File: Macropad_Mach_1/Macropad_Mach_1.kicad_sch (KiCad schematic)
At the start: 39 parts, among them J1 Conn_01x12, J2 Conn_01x12, SW1 RotaryEncoder_Switch_MP

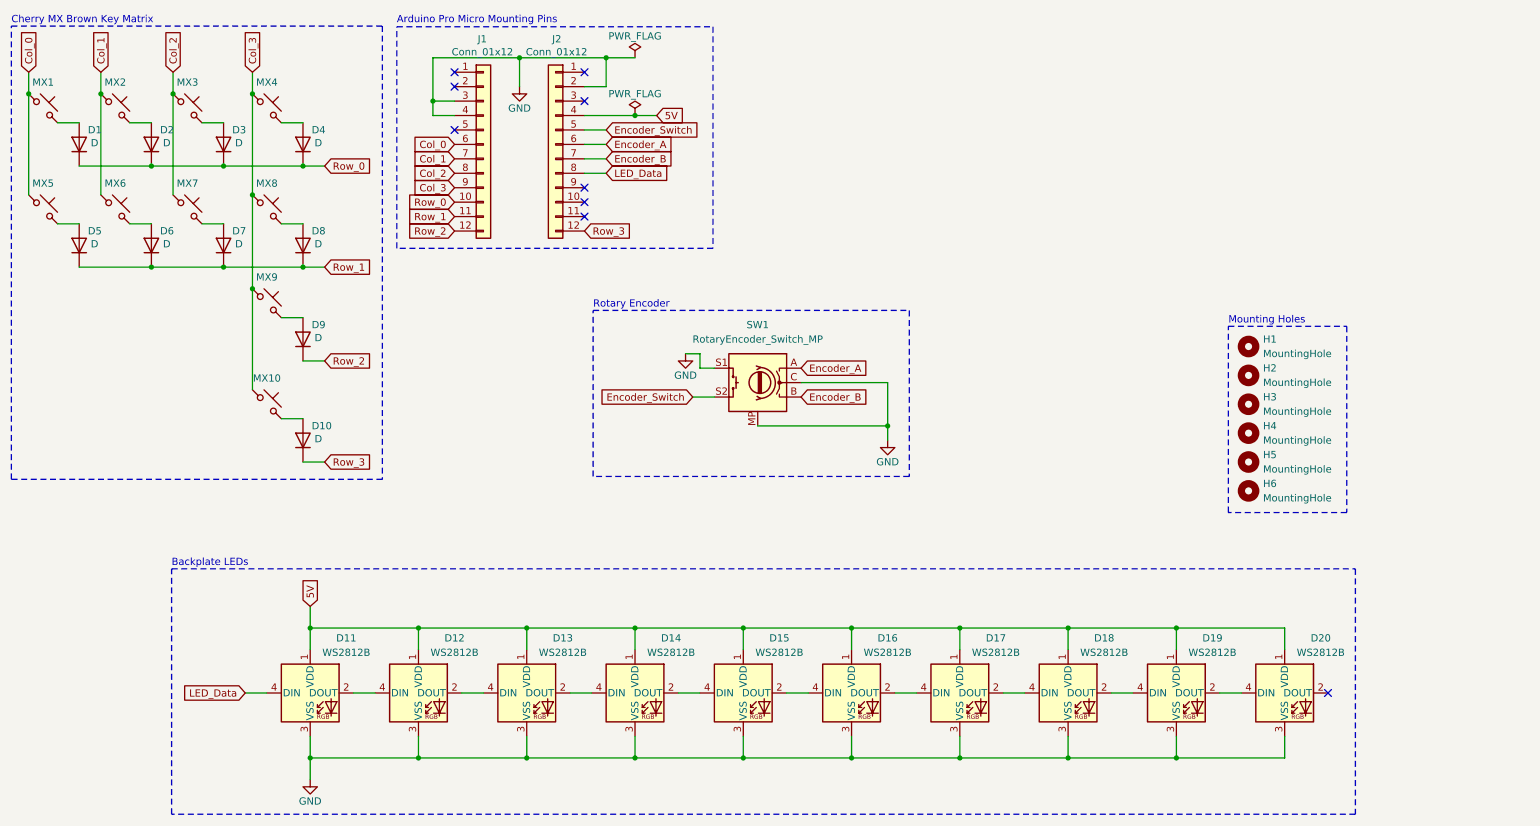
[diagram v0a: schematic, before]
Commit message: feat: update PCB with APA102-2020 LEDs, keyboard layout, and encoder
- Replaced LEDs with APA102-2020
- Created the keyboard layout
- Added Edgecuts
- Routed the keys
- Integrated the encoder into the layout
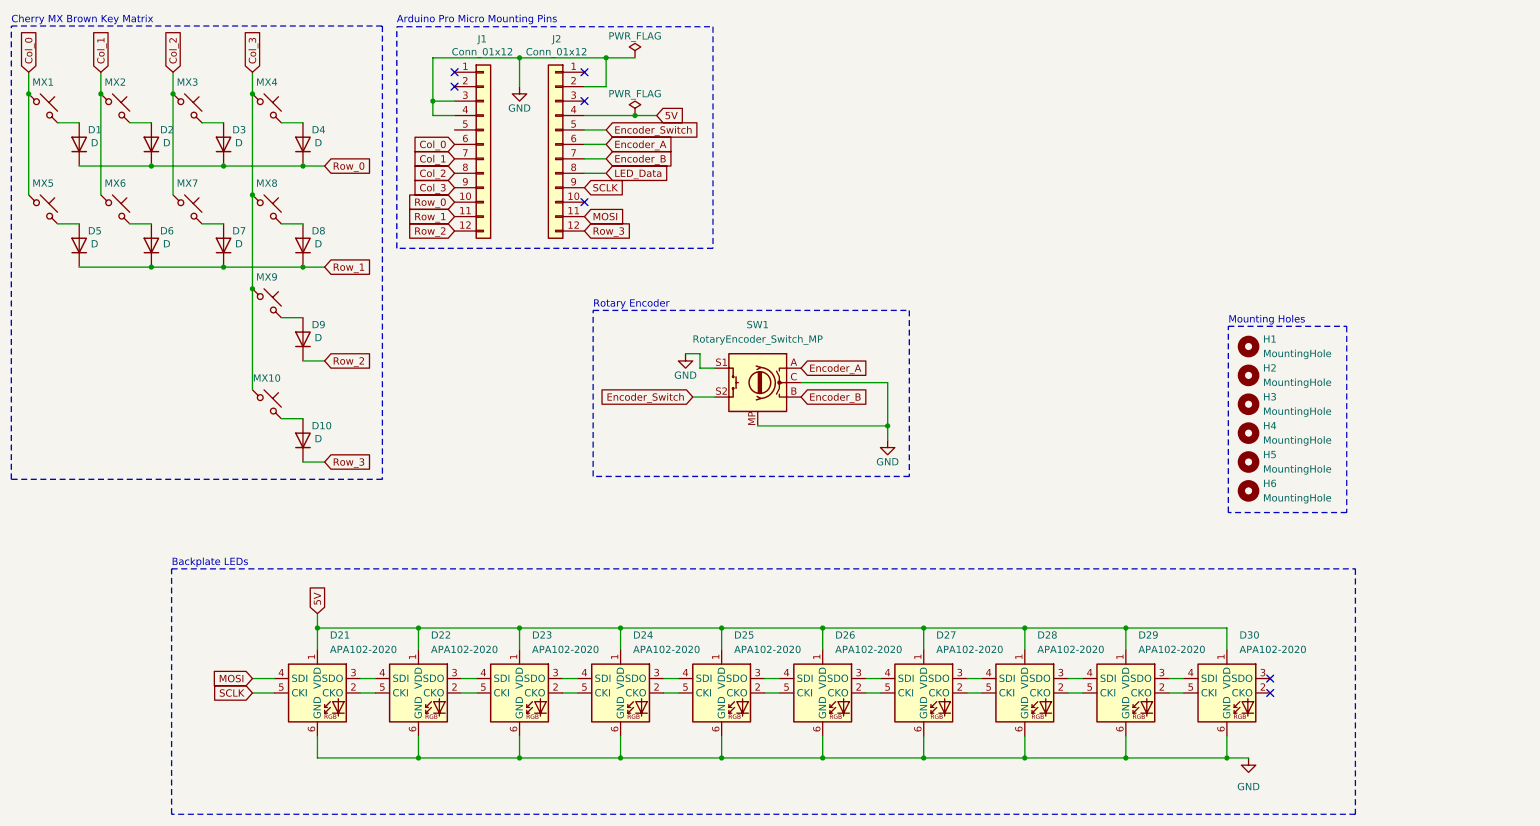
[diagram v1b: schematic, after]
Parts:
- removed D11, D12, D13, D14, D15, D16, D17, D18, D19, D20: WS2812B, LED_SMD:LED_WS2812B_PLCC4_5.0x5.0mm_P3.2mm, symbol LED:WS2812B
- added D21, D22, D23, D24, D25, D26, D27, D28, D29, D30: APA102-2020, LED_SMD:LED-APA102-2020, symbol LED:APA102-2020
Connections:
- net 5V: now also D21.1 (VDD), D22.1 (VDD), D23.1 (VDD), D24.1 (VDD), D25.1 (VDD), D26.1 (VDD), D27.1 (VDD), D28.1 (VDD), D29.1 (VDD), D30.1 (VDD)
- net GND: now also D21.6 (GND), D22.6 (GND), D23.6 (GND), D24.6 (GND), D25.6 (GND), D26.6 (GND), D27.6 (GND), D28.6 (GND), D29.6 (GND), D30.6 (GND)
- net MOSI: now reaches J2.11 (Pin_11)
- net MOSI: now also D21.4 (SDI)
- net SCLK: now reaches J2.9 (Pin_9)
- net SCLK: now also D21.5 (CKI)
- new net: D23.2 (CKO), D24.5 (CKI)
- new net: D23.3 (SDO), D24.4 (SDI)
- new net: D22.3 (SDO), D23.4 (SDI)
- new net: D22.2 (CKO), D23.5 (CKI)
- new net: D27.2 (CKO), D28.5 (CKI)
- new net: D27.3 (SDO), D28.4 (SDI)
- new net: D26.3 (SDO), D27.4 (SDI)
- new net: D26.2 (CKO), D27.5 (CKI)
- new net: D21.2 (CKO), D22.5 (CKI)
- new net: D21.3 (SDO), D22.4 (SDI)
- new net: D25.3 (SDO), D26.4 (SDI)
- new net: D25.2 (CKO), D26.5 (CKI)
- new net: D24.3 (SDO), D25.4 (SDI)
- new net: D24.2 (CKO), D25.5 (CKI)
- new net: D29.3 (SDO), D30.4 (SDI)
- new net: D29.2 (CKO), D30.5 (CKI)
- new net: D28.2 (CKO), D29.5 (CKI)
- new net: D28.3 (SDO), D29.4 (SDI)
- no-connect marks 9 -> 7

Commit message: Finalized PCB routing, connected decoder, and improved design for manufacturing
- Completed trace routing for the keys
- Connected the decoder to the circuit
- Refined silkscreen for better readability
- Adjusted trace widths to meet design requirements
- Optimized clearance settings for JLCPCB manufacturing
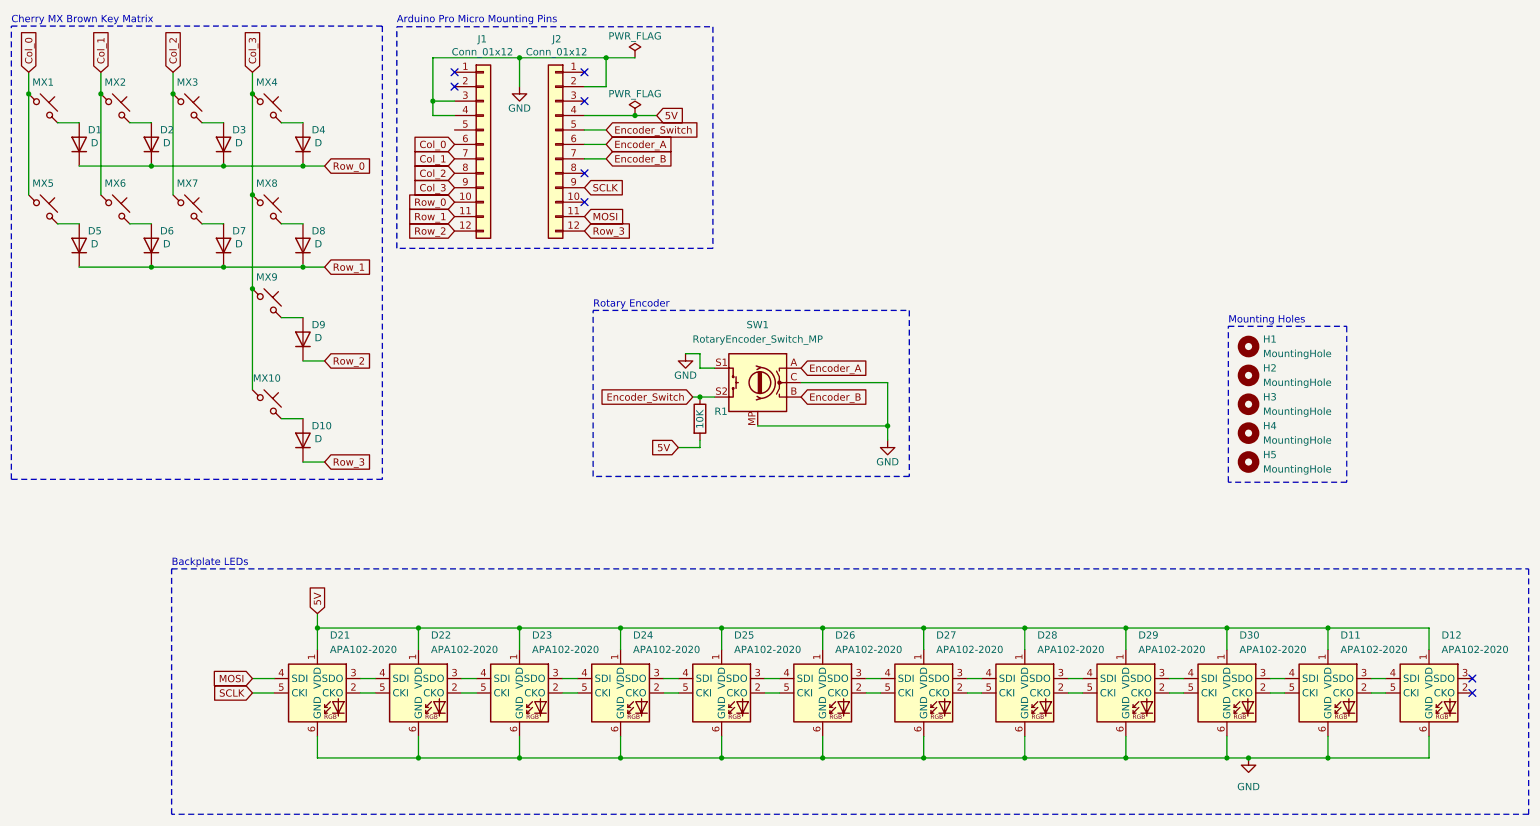
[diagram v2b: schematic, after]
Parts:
- removed H6: MountingHole, MountingHole:MountingHole_3.2mm_M3, symbol Mechanical:MountingHole
- added D11, D12: APA102-2020, LED_SMD:LED-APA102-2020, symbol LED:APA102-2020
- added R1: 10K, Resistor_SMD:R_0603_1608Metric_Pad0.98x0.95mm_HandSolder, symbol Device:R
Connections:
- net 5V: now also D11.1 (VDD), D12.1 (VDD), R1.2
- net Encoder_Switch: now also R1.1
- net GND: now also D11.6 (GND), D12.6 (GND)
- net at D30.2 (CKO): now also D11.5 (CKI)
- net at D30.3 (SDO): now also D11.4 (SDI)
- net LED_Data: no longer names the net of J2.8 (Pin_8)
- new net: D11.2 (CKO), D12.5 (CKI)
- new net: D11.3 (SDO), D12.4 (SDI)
- no-connect marks 7 -> 8

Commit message: Feat: added Logoand Description
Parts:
- added C1: 4.7 µF, Capacitor_SMD:C_0201_0603Metric_Pad0.64x0.40mm_HandSolder, symbol Device:C
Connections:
- net 5V: now also C1.2
- net GND: now also C1.1
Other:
- note added: "LED Decoupling Cap"
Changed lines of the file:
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@@
 	(wire
 		(pts
+			(xy 148.59 25.4) (xy 148.59 34.29)
+		)
+		(stroke
+			(width 0)
+			(type default)
+		)
+	)
+	(wire
+		(pts
 			(xy 104.14 144.78) (xy 86.36 144.78)
 		)
@@
 	(wire
 		(pts
+			(xy 153.67 25.4) (xy 148.59 25.4)
+		)
+		(stroke
+			(width 0)
+			(type default)
+		)
+	)
+	(wire
+		(pts
 			(xy 232.41 144.78) (xy 246.38 144.78)
 		)
@@
 	(wire
 		(pts
+			(xy 153.67 34.29) (xy 153.67 33.02)
+		)
+		(stroke
+			(width 0)
+			(type default)
+		)
+	)
+	(wire
+		(pts
 			(xy 57.15 27.94) (xy 57.15 45.72)
 		)
@@
 	(wire
 		(pts
+			(xy 156.21 34.29) (xy 153.67 34.29)
+		)
+		(stroke
+			(width 0)
+			(type default)
+		)
+	)
+	(wire
+		(pts
 			(xy 68.58 140.97) (xy 68.58 144.78)
 		)
@@
 	)
 	(rectangle
+		(start 145.796 24.13)
+		(end 162.052 40.132)
+		(stroke
+			(width 0)
+			(type dash_dot)
+		)
+		(fill
+			(type none)
+		)
+	)
+	(rectangle
 		(start 42.926 111.506)
 		(end 281.686 154.686)
@@
 		)
 	)
+	(text "LED Decoupling Cap"
+		(exclude_from_sim no)
+		(at 145.796 22.86 0)
+		(effects
+			(font
+				(size 1.27 1.27)
+			)
+			(justify left)
+		)
+	)
 	(text "Rotary Encoder \n"
 		(exclude_from_sim no)
@@
 		)
 	)
+	(global_label "5V"
+		(shape input)
+		(at 156.21 34.29 0)
+		(fields_autoplaced yes)
+		(effects
+			(font
+				(size 1.27 1.27)
+			)
+			(justify left)
+		)
+		(property "Intersheetrefs" "${INTERSHEET_REFS}"
+			(at 161.4933 34.29 0)
+			(effects
+				(font
+					(size 1.27 1.27)
+				)
+				(justify left)
+				(hide yes)
+			)
+		)
+	)
 	(global_label "Row_2"
 		(shape input)
@@
 	)
 	(symbol
+		(lib_id "Device:C")
+		(at 153.67 29.21 0)
+		(unit 1)
+		(exclude_from_sim no)
+		(in_bom yes)
+		(on_board yes)
+		(dnp no)
+		(property "Reference" "C1"
+			(at 150.368 26.924 0)
+			(effects
+				(font
+					(size 1.27 1.27)
+				)
+				(justify left)
+			)
+		)
+		(property "Value" "4.7 µF"
+			(at 154.178 26.924 0)
+			(effects
+				(font
+					(size 1.27 1.27)
+				)
+				(justify left)
+			)
+		)
+		(property "Footprint" "Capacitor_SMD:C_0201_0603Metric_Pad0.64x0.40mm_HandSolder"
+			(at 154.6352 33.02 0)
+			(effects
+				(font
+					(size 1.27 1.27)
+				)
+				(hide yes)
+			)
+		)
+		(property "Datasheet" "~"
+			(at 153.67 29.21 0)
+			(effects
+				(font
+					(size 1.27 1.27)
+				)
+				(hide yes)
+			)
+		)
+		(property "Description" "Unpolarized capacitor"
+			(at 153.67 29.21 0)
+			(effects
+				(font
+					(size 1.27 1.27)
+				)
+				(hide yes)
+			)
+		)
+		(pin "2"
+		)
+		(pin "1"
+		)
+		(instances
+			(project ""
+				(path "/0abaf165-01a1-44d2-a38f-248e4be66f95"
+					(reference "C1")
+					(unit 1)
+				)
+			)
+		)
+	)
+	(symbol
 		(lib_id "Mechanical:MountingHole")
 		(at 232.41 82.55 0)
@@
 					(unit 1)
 				)
+			)
+		)
+	)
+	(symbol
+		(lib_id "power:GND")
+		(at 148.59 34.29 0)
+		(mirror y)
+		(unit 1)
+		(exclude_from_sim no)
+		(in_bom yes)
+		(on_board yes)
+		(dnp no)
+		(property "Reference" "#PWR04"
+			(at 148.59 40.64 0)
+			(effects
+				(font
+					(size 1.27 1.27)
+				)
+				(hide yes)
+			)
+		)
+		(property "Value" "GND"
+			(at 148.59 38.1 0)
+			(effects
+				(font
+					(size 1.27 1.27)
+				)
+			)
+		)
+		(property "Footprint" ""
+			(at 148.59 34.29 0)
+			(effects
+				(font
+					(size 1.27 1.27)
+				)
+				(hide yes)
+			)
+		)
+		(property "Datasheet" ""
+			(at 148.59 34.29 0)
+			(effects
+				(font
+					(size 1.27 1.27)
+				)
+				(hide yes)
+			)
+		)
+		(property "Description" "Power symbol creates a global label with name \"GND\" , ground"
+			(at 148.59 34.29 0)
+			(effects
+				(font
+					(size 1.27 1.27)
+				)
+				(hide yes)
+			)
+		)
+		(pin "1"
+		)
+		(instances
+			(project "Macropad_Mach_1"
+				(path "/0abaf165-01a1-44d2-a38f-248e4be66f95"
+					(reference "#PWR04")
+					(unit 1)
+				)
